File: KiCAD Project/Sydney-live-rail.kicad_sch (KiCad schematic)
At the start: 69 parts, among them J1 Prog Connector, Q1 HL3415A, Q2 MMBT3904, U1 RT9080-33GJ5, U2 ESP32-C3FH4, U3 LTR-303ALS-01, U4 Connector, USB-TYPE-C-16P, U5 SN74LV1T34DBV, X1 40MHz, 15pF

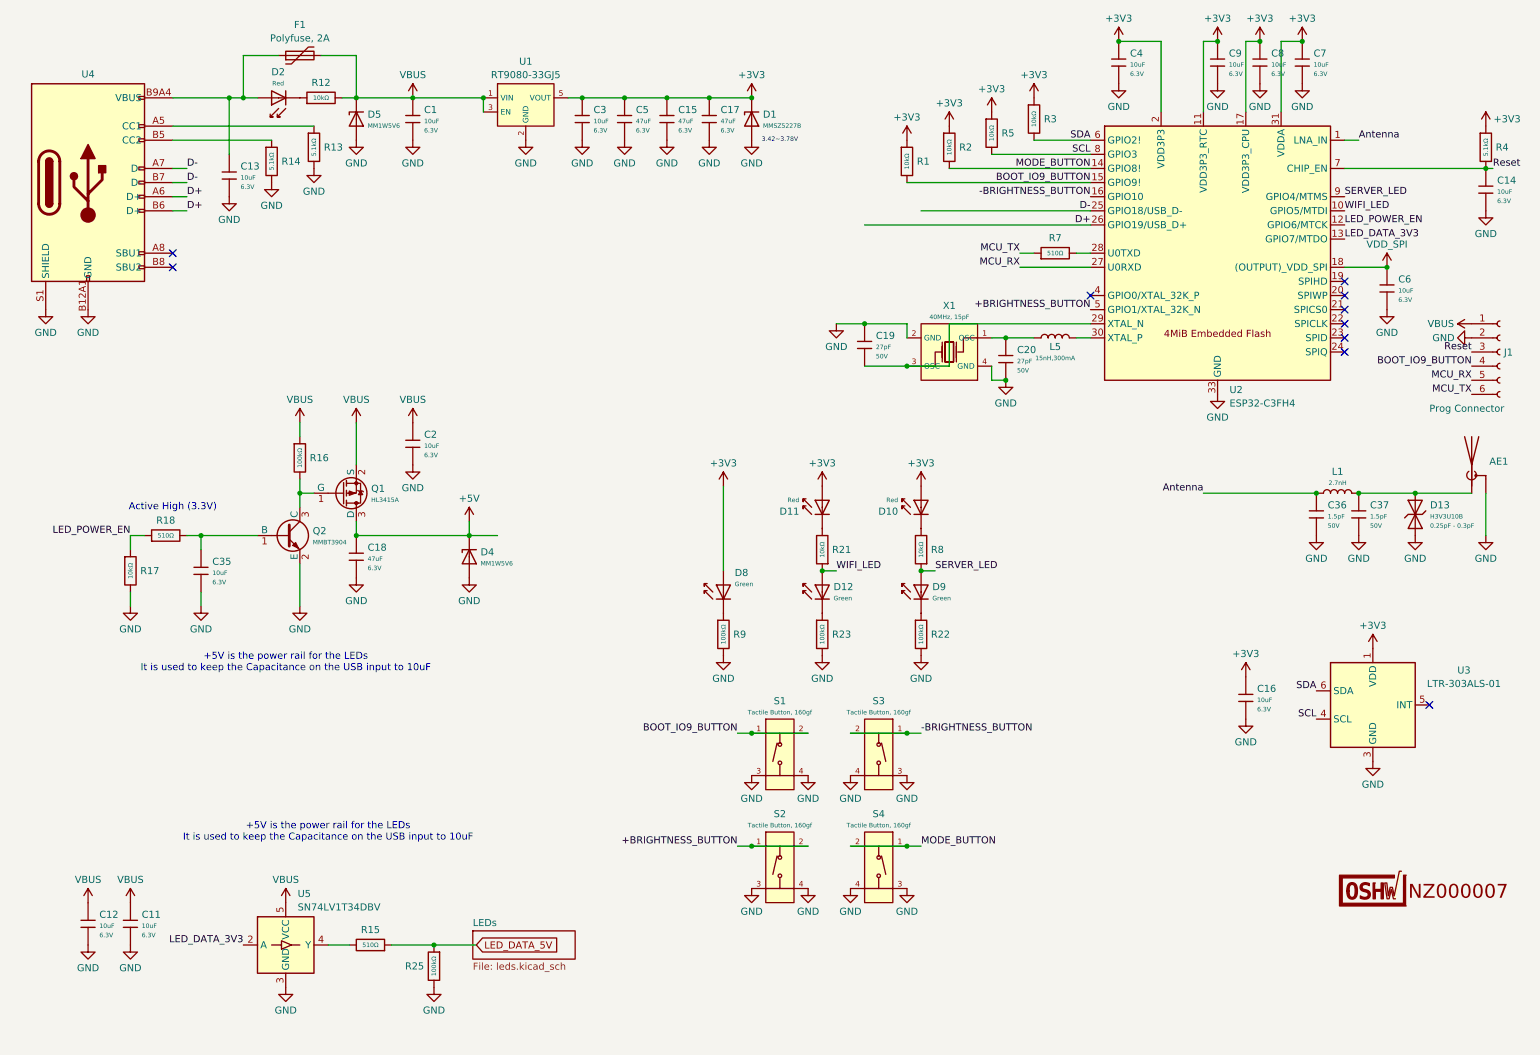
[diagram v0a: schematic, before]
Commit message: Added annotations to schematic
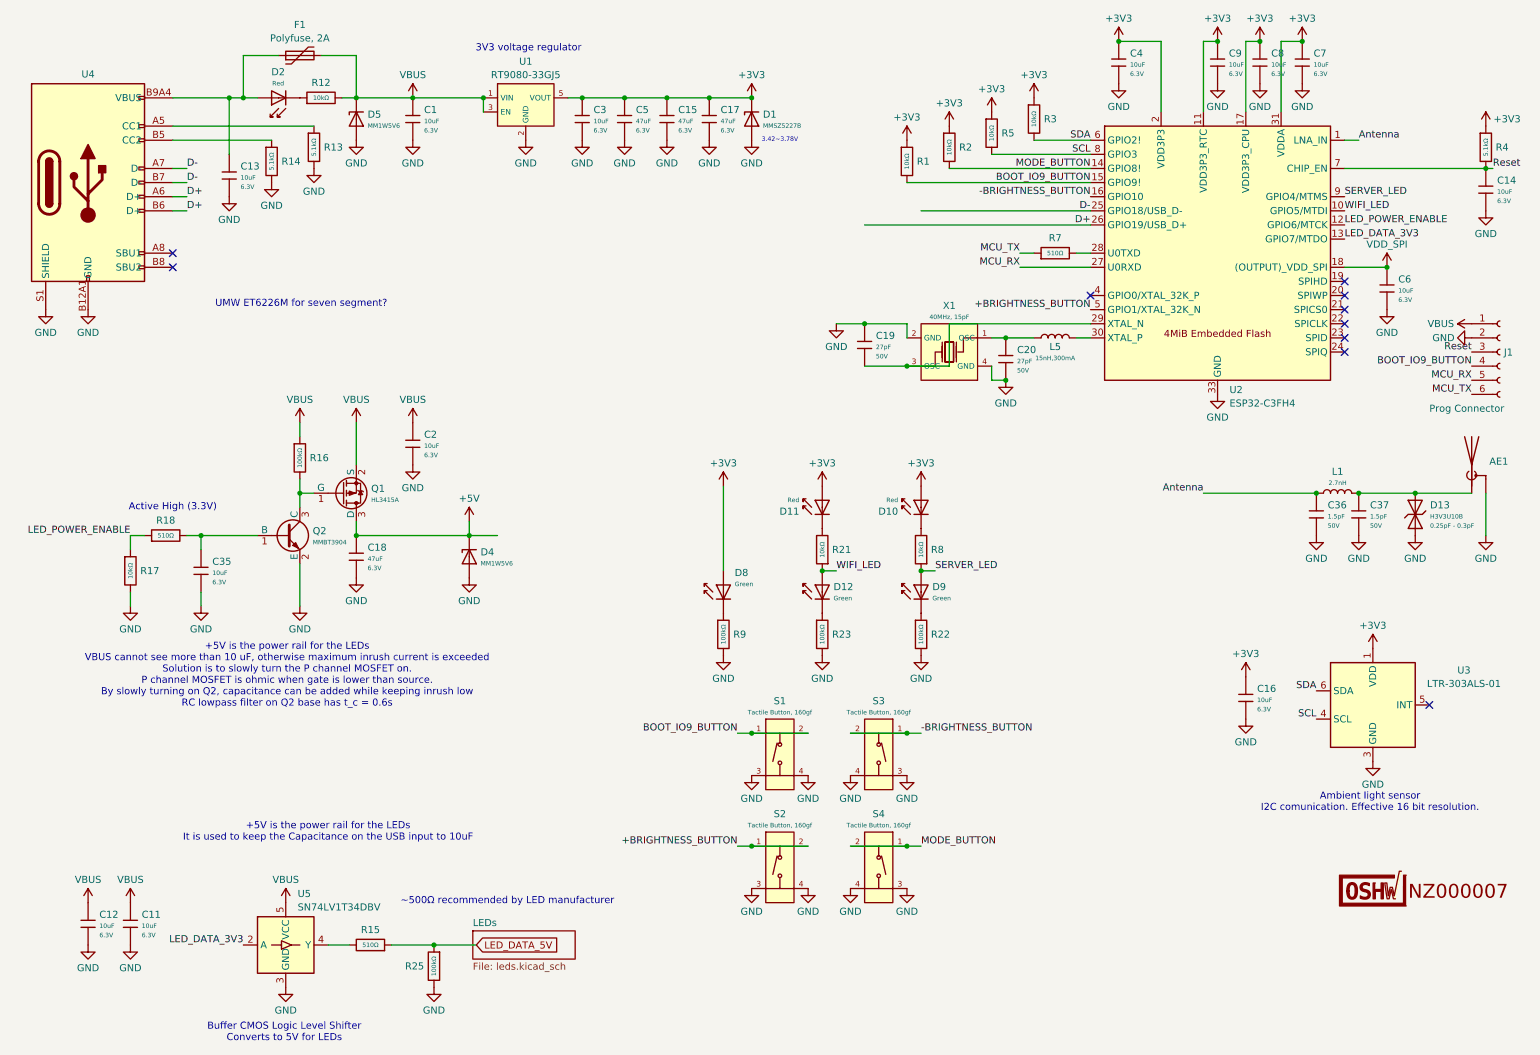
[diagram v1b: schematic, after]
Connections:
- net LED_POWER_EN renamed LED_POWER_ENABLE
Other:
- note added: "+5V is the power rail for the LEDs VBUS cannot see more than 10 uF, otherwise maximum inrush current is exceeded Solution is to slowly turn the P channel MOSFET on. P channel MOSFET is ohmic when gate is lower than source. By slowly turning on Q2, capacitance can be added while keeping inrush low RC lowpass filter on Q2 base has t_c = 0.6s"
- note added: "3V3 voltage regulator"
- note added: "Ambient light sensor I2C comunication. Effective 16 bit resolution."
- note added: "Buffer CMOS Logic Level Shifter Converts to 5V for LEDs"
- note added: "UMW ET6226M for seven segment?"
- note added: "~500Ω recommended by LED manufacturer"
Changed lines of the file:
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@@
 		)
 	)
-	(text "+5V is the power rail for the LEDs\nIt is used to keep the Capacitance on the USB input to 10uF"
+	(text "+5V is the power rail for the LEDs\nVBUS cannot see more than 10 uF, otherwise maximum inrush current is exceeded\nSolution is to slowly turn the P channel MOSFET on.\nP channel MOSFET is ohmic when gate is lower than source.\nBy slowly turning on Q2, capacitance can be added while keeping inrush low\nRC lowpass filter on Q2 base has t_c = 0.6s"
 		(exclude_from_sim no)
-		(at 60.96 129.54 0)
+		(at 61.214 131.826 0)
+		(effects
+			(font
+				(size 1.27 1.27)
+			)
+		)
+	)
+	(text "Ambient light sensor\nI2C comunication. Effective 16 bit resolution."
+		(exclude_from_sim no)
+		(at 256.032 154.686 0)
+		(effects
+			(font
+				(size 1.27 1.27)
+			)
+		)
+	)
+	(text "UMW ET6226M for seven segment?\n"
+		(exclude_from_sim no)
+		(at 63.754 65.024 0)
+		(effects
+			(font
+				(size 1.27 1.27)
+			)
+		)
+	)
+	(text "3V3 voltage regulator"
+		(exclude_from_sim no)
+		(at 104.648 19.05 0)
+		(effects
+			(font
+				(size 1.27 1.27)
+			)
+		)
+	)
+	(text "Buffer CMOS Logic Level Shifter\nConverts to 5V for LEDs"
+		(exclude_from_sim no)
+		(at 60.706 196.088 0)
 		(effects
 			(font
@@
 			(font
 				(size 0.8 0.8)
+			)
+		)
+	)
+	(text "~500Ω recommended by LED manufacturer\n"
+		(exclude_from_sim no)
+		(at 100.838 172.466 0)
+		(effects
+			(font
+				(size 1.27 1.27)
 			)
 		)
@@
 		)
 	)
-	(label "LED_POWER_EN"
+	(label "LED_POWER_ENABLE"
 		(at 251.46 50.8 0)
 		(effects
@@
 		)
 	)
-	(label "LED_POWER_EN"
+	(label "LED_POWER_ENABLE"
 		(at 33.02 106.68 180)
 		(effects

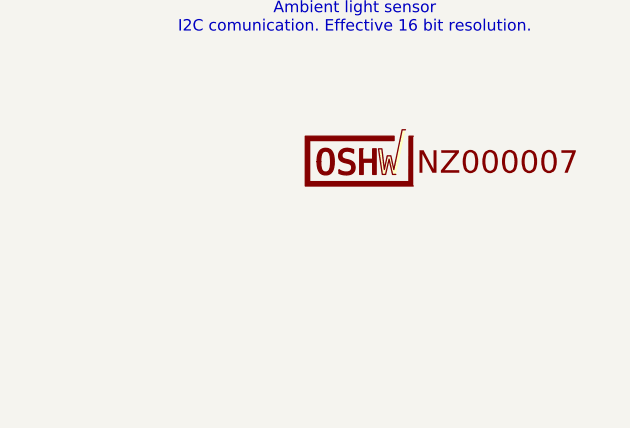
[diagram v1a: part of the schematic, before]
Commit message: Added control electronics from Wellington project
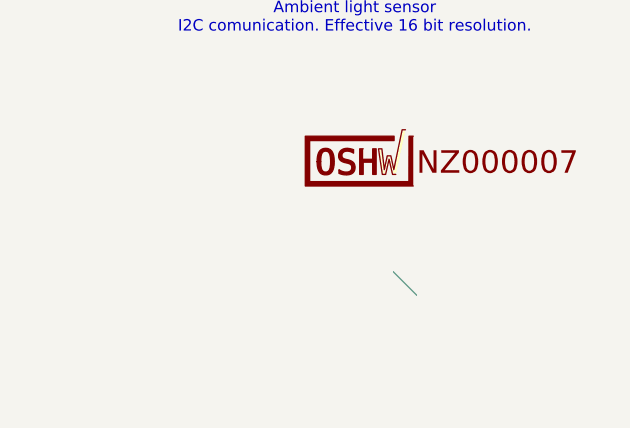
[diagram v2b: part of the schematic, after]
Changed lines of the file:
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@@
 		(at 40.64 55.88)
+	)
+	(bus_entry
+		(at 260.35 182.88)
+		(size 2.54 2.54)
+		(stroke
+			(width 0)
+			(type default)
+		)
 	)
 	(wire
